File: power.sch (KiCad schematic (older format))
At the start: 57 parts, among them J11 Conn_01x03, J12 Conn_01x01_Male, J5 Conn_01x02, Q2 TSM085P03CV RGG, Q3 Q_NMOS_GSD, U7 MP2636GR-P, U8 NCP133AMX150TCG

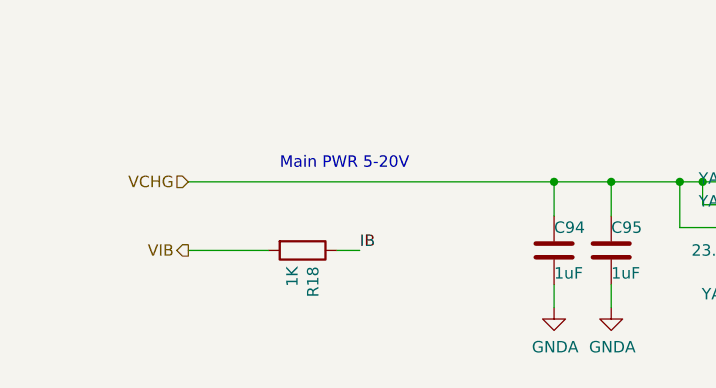
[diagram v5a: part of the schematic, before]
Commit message: Add header for main power input
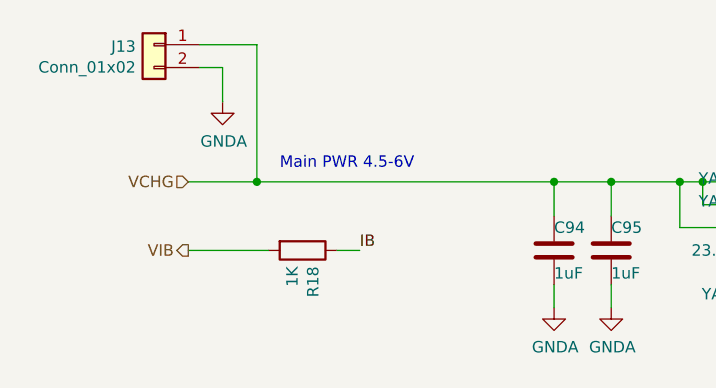
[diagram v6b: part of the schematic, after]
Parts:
- added J13: Conn_01x02, Connector_PinHeader_1.27mm:PinHeader_1x02_P1.27mm_Horizontal, symbol Connector_Generic:Conn_01x02
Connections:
- net GND: now also J13.2 (Pin_2)
- net VCHG: now also J13.1 (Pin_1)
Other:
- note added: "Main PWR 4.5-6V"
- note removed: "Main PWR 5-20V"
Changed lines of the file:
@@
 5V 3A
 Text Notes 2350 2350 0    50   ~ 0
-Main PWR 5-20V
+Main PWR 4.5-6V
 $Comp
 L power:GND #PWR0170
@@
 $EndComp
 Wire Wire Line
-	1950 2400 3550 2400
+	1950 2400 2250 2400
 Text Label 9050 3100 0    50   ~ 0
 FB_DIV
@@
 Text Notes 10800 7550 0    50   ~ 0
 Fake\nRNTC
+$Comp
+L Connector_Generic:Conn_01x02 J?
+U 1 1 5F9E7E0C
+P 1800 1800
+AR Path="/5F9E7E0C" Ref="J?"  Part="1"
+AR Path="/5DC6F4F1/5F9E7E0C" Ref="J13"  Part="1"
+F 0 "J13" H 1880 1792 50  0000 L CNN
+F 1 "Conn_01x02" H 1880 1701 50  0000 L CNN
+F 2 "Connector_PinHeader_1.27mm:PinHeader_1x02_P1.27mm_Horizontal" H 1800 1800 50  0001 C CNN
+F 3 "~" H 1800 1800 50  0001 C CNN
+	1    1800 1800
+	-1   0    0    -1
+$EndComp
+Wire Wire Line
+	2000 1800 2250 1800
+Wire Wire Line
+	2250 1800 2250 2400
+Connection ~ 2250 2400
+Wire Wire Line
+	2250 2400 3550 2400
+$Comp
+L power:GNDA #PWR0275
+U 1 1 5FA37EDE
+P 2100 2050
+F 0 "#PWR0275" H 2100 1800 50  0001 C CNN
+F 1 "GNDA" H 2105 1877 50  0000 C CNN
+F 2 "" H 2100 2050 50  0001 C CNN
+F 3 "" H 2100 2050 50  0001 C CNN
+	1    2100 2050
+	1    0    0    -1
+$EndComp
+Wire Wire Line
+	2100 2050 2100 1900
+Wire Wire Line
+	2100 1900 2000 1900
 $EndSCHEMATC

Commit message: Set up for battery NTC and add a power button
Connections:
- net VCHG: no longer J13.1 (Pin_1)
- net VSYS_5V: now also J13.1 (Pin_1)
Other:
- moved on the sheet: J13
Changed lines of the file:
@@
 EESchema Schematic File Version 4
-LIBS:mxenc-cache
-EELAYER 29 0
+EELAYER 30 0
 EELAYER END
 $Descr USLedger 17000 11000
 encoding utf-8
 Sheet 6 10
-Title ""
-Date ""
-Rev ""
-Comp ""
+Title "kimχ micro"
+Date "2020-03-05"
+Rev "0.9"
+Comp "GroupGets"
 Comment1 ""
 Comment2 ""
@@
 	10150 3100 9900 3100
 Wire Wire Line
-	14150 2400 11250 2400
+	14150 2400 13250 2400
 $Comp
 L Device:Q_NMOS_GSD Q3
@@
 Connection ~ 11500 3550
 Connection ~ 11250 2400
-Wire Wire Line
-	11250 2400 11150 2400
 Wire Wire Line
 	11500 3150 11500 3050
@@
 Wire Wire Line
 	12450 3050 12550 3050
-$Comp
-L power:PWR_FLAG #FLG0102
-U 1 1 5DE60E1E
-P 11150 2400
-F 0 "#FLG0102" H 11150 2475 50  0001 C CNN
-F 1 "PWR_FLAG" H 11150 2573 50  0000 C CNN
-F 2 "" H 11150 2400 50  0001 C CNN
-F 3 "~" H 11150 2400 50  0001 C CNN
-	1    11150 2400
-	1    0    0    -1
-$EndComp
-Connection ~ 11150 2400
 Text Label 7250 2800 0    50   ~ 0
 SW
@@
 Connection ~ 10650 2400
 Wire Wire Line
-	10650 2400 11150 2400
-Wire Wire Line
 	10150 3100 10400 3100
 Wire Wire Line
@@
 	0    1    1    0
 $EndComp
-Wire Wire Line
-	1950 2400 2250 2400
 Text Label 9050 3100 0    50   ~ 0
 FB_DIV
@@
 L Connector_Generic:Conn_01x02 J?
 U 1 1 5F9E7E0C
-P 1800 1800
+P 12800 1800
 AR Path="/5F9E7E0C" Ref="J?"  Part="1"
 AR Path="/5DC6F4F1/5F9E7E0C" Ref="J13"  Part="1"
-F 0 "J13" H 1880 1792 50  0000 L CNN
-F 1 "Conn_01x02" H 1880 1701 50  0000 L CNN
-F 2 "Connector_PinHeader_1.27mm:PinHeader_1x02_P1.27mm_Horizontal" H 1800 1800 50  0001 C CNN
-F 3 "~" H 1800 1800 50  0001 C CNN
-	1    1800 1800
+F 0 "J13" H 12880 1792 50  0000 L CNN
+F 1 "Conn_01x02" H 12880 1701 50  0000 L CNN
+F 2 "Connector_PinHeader_1.27mm:PinHeader_1x02_P1.27mm_Horizontal" H 12800 1800 50  0001 C CNN
+F 3 "~" H 12800 1800 50  0001 C CNN
+	1    12800 1800
 	-1   0    0    -1
 $EndComp
 Wire Wire Line
-	2000 1800 2250 1800
-Wire Wire Line
-	2250 1800 2250 2400
-Connection ~ 2250 2400
-Wire Wire Line
-	2250 2400 3550 2400
+	13000 1800 13250 1800
+Wire Wire Line
+	13250 1800 13250 2400
 $Comp
 L power:GNDA #PWR0275
 U 1 1 5FA37EDE
-P 2100 2050
-F 0 "#PWR0275" H 2100 1800 50  0001 C CNN
-F 1 "GNDA" H 2105 1877 50  0000 C CNN
-F 2 "" H 2100 2050 50  0001 C CNN
-F 3 "" H 2100 2050 50  0001 C CNN
-	1    2100 2050
-	1    0    0    -1
-$EndComp
-Wire Wire Line
-	2100 2050 2100 1900
-Wire Wire Line
-	2100 1900 2000 1900
+P 13100 2050
+F 0 "#PWR0275" H 13100 1800 50  0001 C CNN
+F 1 "GNDA" H 13105 1877 50  0000 C CNN
+F 2 "" H 13100 2050 50  0001 C CNN
+F 3 "" H 13100 2050 50  0001 C CNN
+	1    13100 2050
+	1    0    0    -1
+$EndComp
+Wire Wire Line
+	13100 2050 13100 1900
+Wire Wire Line
+	13100 1900 13000 1900
+Connection ~ 13250 2400
+Wire Wire Line
+	13250 2400 11250 2400
+Wire Wire Line
+	1950 2400 3550 2400
+Wire Wire Line
+	10650 2400 11250 2400
 $EndSCHEMATC

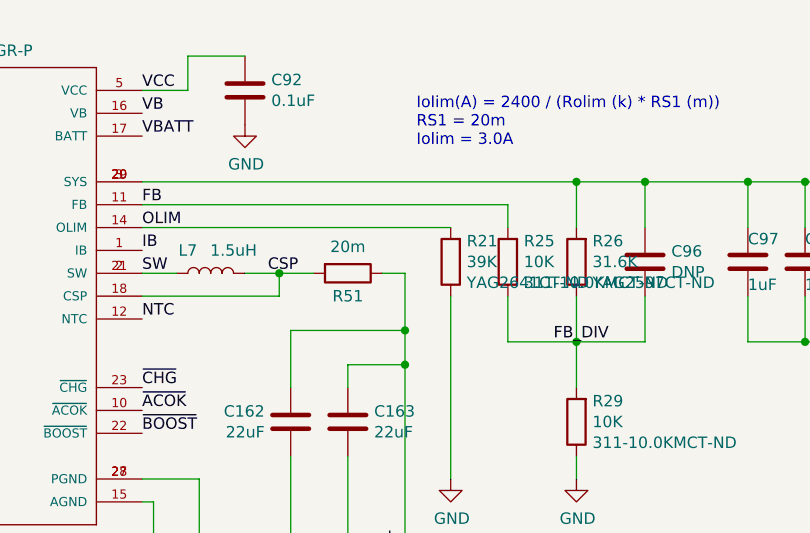
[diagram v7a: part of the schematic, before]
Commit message: Cleanup remaining DRC problems from schematic
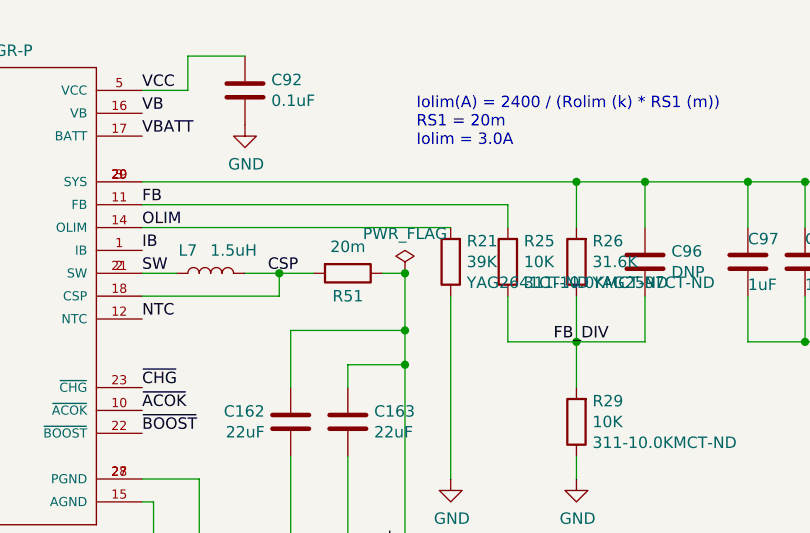
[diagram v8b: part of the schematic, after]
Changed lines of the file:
@@
 1A charge\ncurrent
-Wire Wire Line
-	7700 2800 7850 2800
 Wire Wire Line
 	8150 3300 8150 3200
@@
 Wire Wire Line
 	7450 2000 7450 1850
-Wire Wire Line
-	7450 1850 7700 1850
 $Comp
 L Device:C C92
@@
 	6450 5250 6450 5100
 Wire Wire Line
-	6450 5100 6700 5100
-Wire Wire Line
 	6700 5100 6700 5250
 Text Label 7250 3300 0    50   ~ 0
@@
 Wire Wire Line
 	10650 2400 11250 2400
+Wire Wire Line
+	6450 5100 6700 5100
+Wire Wire Line
+	7450 1850 7700 1850
+$Comp
+L power:PWR_FLAG #FLG0102
+U 1 1 5E7B504E
+P 8400 2800
+F 0 "#FLG0102" H 8400 2875 50  0001 C CNN
+F 1 "PWR_FLAG" H 8400 2973 50  0000 C CNN
+F 2 "" H 8400 2800 50  0001 C CNN
+F 3 "~" H 8400 2800 50  0001 C CNN
+	1    8400 2800
+	1    0    0    -1
+$EndComp
+Connection ~ 8400 2800
+Wire Wire Line
+	7700 2800 7850 2800
 $EndSCHEMATC
